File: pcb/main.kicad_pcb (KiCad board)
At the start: 2 copper layers, 257 x 76.2 mm, 110 parts, among them J1 Barrel_Jack, J2 NXC digit iface, J3 NXC num iface, J4 Conn_01x03, J5 ICSP, J6 Conn_02x06_Counter_Clockwise, J7 Conn_02x12_Counter_Clockwise, Q1 IRF740, Q10 ZVP1320F, Q11 BSS127S, Q12 ZVN3320F, Q13 BSS127S, Q14 BSS127S, Q15 ZVP1320F, Q16 BSS127S, Q17 BSS127S, Q18 ZVN3320F, Q19 BSS127S, Q2 ZVN3320F, Q20 ZVP1320F, Q3 BSS127S, Q4 ZVP1320F, Q5 BSS127S, Q6 BSS127S, Q7 ZVN3320F, Q8 BSS127S, Q9 BSS127S, SW1 Tactile SPST, SW2 Tactile SPST, SW3 Tactile SPST, U1 4028, U2 NCP1117-5.0_SOT223, U3 PIC24FV32KA302-I_SO, U4 DS1307Z+, U5 MAX1771, Y1 8 MHz, Y2 32.768 kHz

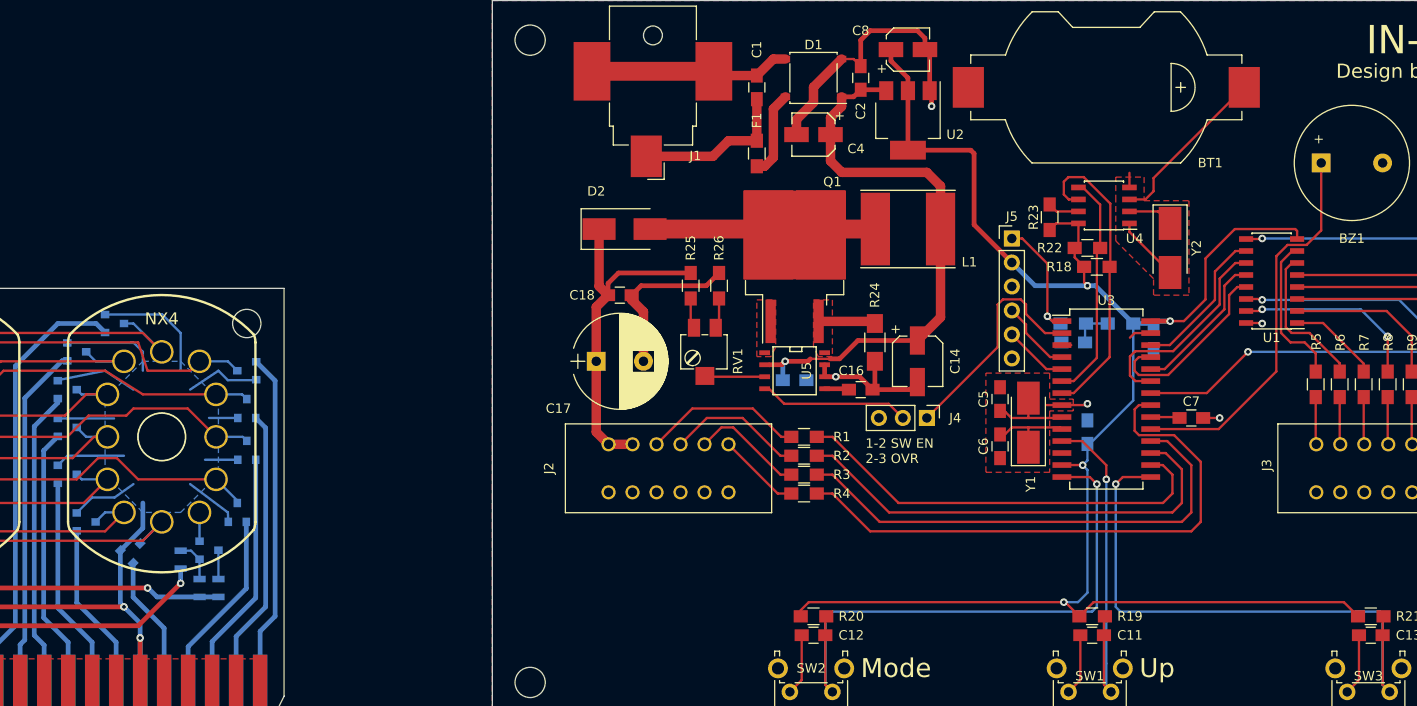
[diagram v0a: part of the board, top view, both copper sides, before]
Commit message: Update PCB and schematic files with mostly small tweaks. Added DRC rules added to .pro, and changes on layout and footprints to reflect that.
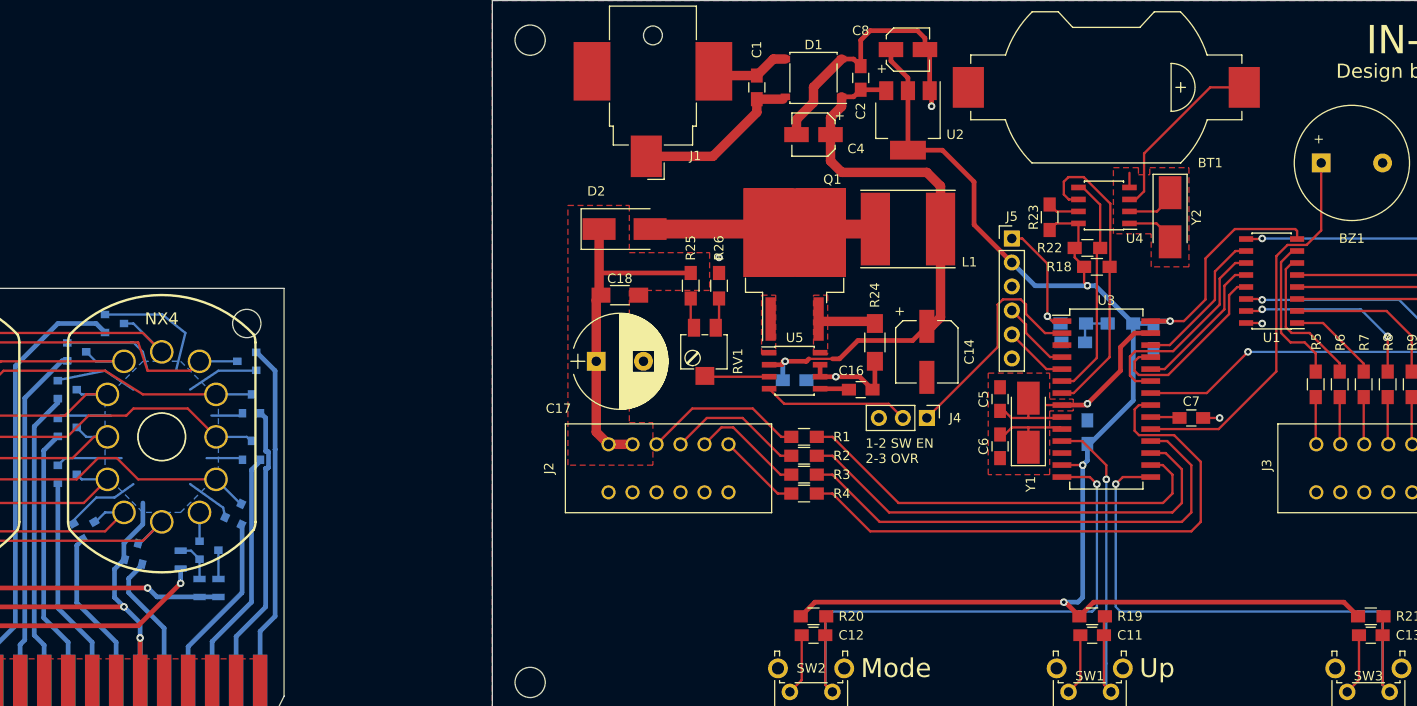
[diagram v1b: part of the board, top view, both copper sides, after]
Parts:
- removed F1: 1.5A, Resistors_SMD:R_0805_HandSoldering
- C14: footprint Capacitors_SMD:CP_Elec_5x5.3 -> Capacitors_SMD:CP_Elec_6.3x7.7
- C18: footprint Capacitors_SMD:C_0805_HandSoldering -> Capacitors_SMD:C_1206_HandSoldering
- R18, R22: value 33k -> 4.7k
- U1: value 4028 -> CD4028
- U2: value NCP1117-5.0_SOT223 -> NCP1117
- U5: footprint SMD_Packages:SOIC-8-N -> Housings_SOIC:SOIC-8_3.9x4.9mm_Pitch1.27mm
- moved Y2 3.25 mm to (221.8, 76.8)
- moved C14 1.41 mm to (196.0, 91.0)
- moved Q13 1.00 mm to (124.0, 92.0)
- moved Q14 0.71 mm to (124.5, 96.5)
- moved Q16 0.50 mm to (124.5, 101.4)
- moved Q3 0.50 mm to (107.0, 109.5), turned to 30 degrees
- moved Q19 0.35 mm to (112.2, 112.2), turned to 75 degrees
- moved Q1 0.25 mm to (182.0, 81.8)
- turned Q17 to 65 degrees
- turned U5 to 0 degrees
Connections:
- D1 pad 4: Net-(D1-Pad4) -> Net-(C1-Pad1)
- J1 pad 3: Net-(C1-Pad2) -> Net-(J1-Pad3)
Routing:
- net /GND: track 94.3 -> 80.8 mm, vias 5 -> 6
- net Net-(C1-Pad2): track 21.4 -> 8.49 mm
- net Net-(D1-Pad4): track 9.09 -> 0.00 mm
- net /+5V: track 183.6 -> 181.1 mm
- net Net-(U4-Pad1): track 6.98 -> 5.41 mm
- net Net-(BT1-Pad1): track 17.9 -> 19.4 mm
- net Net-(C1-Pad1): track 16.8 -> 18.2 mm
- net /+170V: track 37.2 -> 35.9 mm
- net /Tube Board/K7: track 35.4 -> 36.5 mm
- net /Tube Board/GND: track 206.8 -> 207.9 mm
- net Net-(U3-Pad3): track 0.98 -> 0.00 mm
- net /Tube Board/K1: track 17.8 -> 16.9 mm
- net /Tube Board/K8: track 29.7 -> 30.5 mm
- net /+RAW: track 61.3 -> 62.1 mm
- net /Tube Board/K_DP: track 14.0 -> 14.7 mm
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
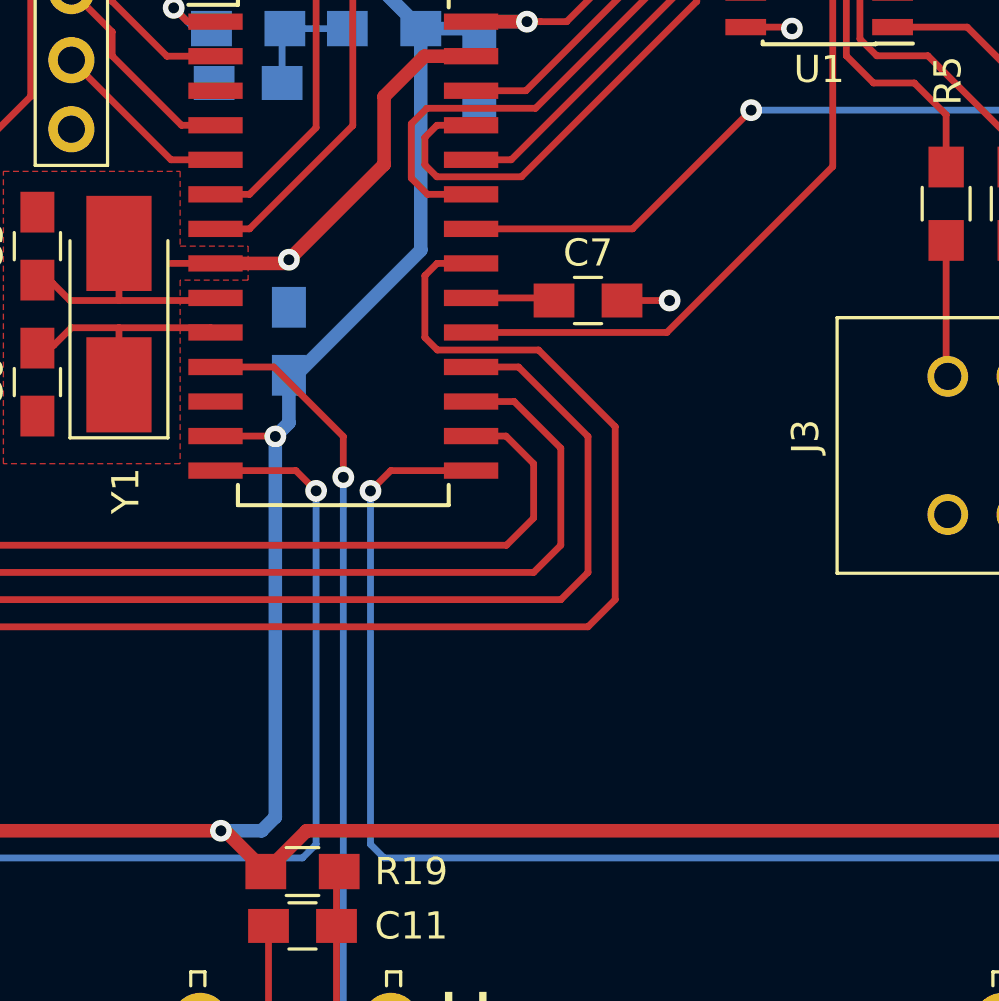
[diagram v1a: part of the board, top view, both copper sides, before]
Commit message: Add alternate parts for BOM, adjust micro to be more compatible with new PIC24FJ series parts.
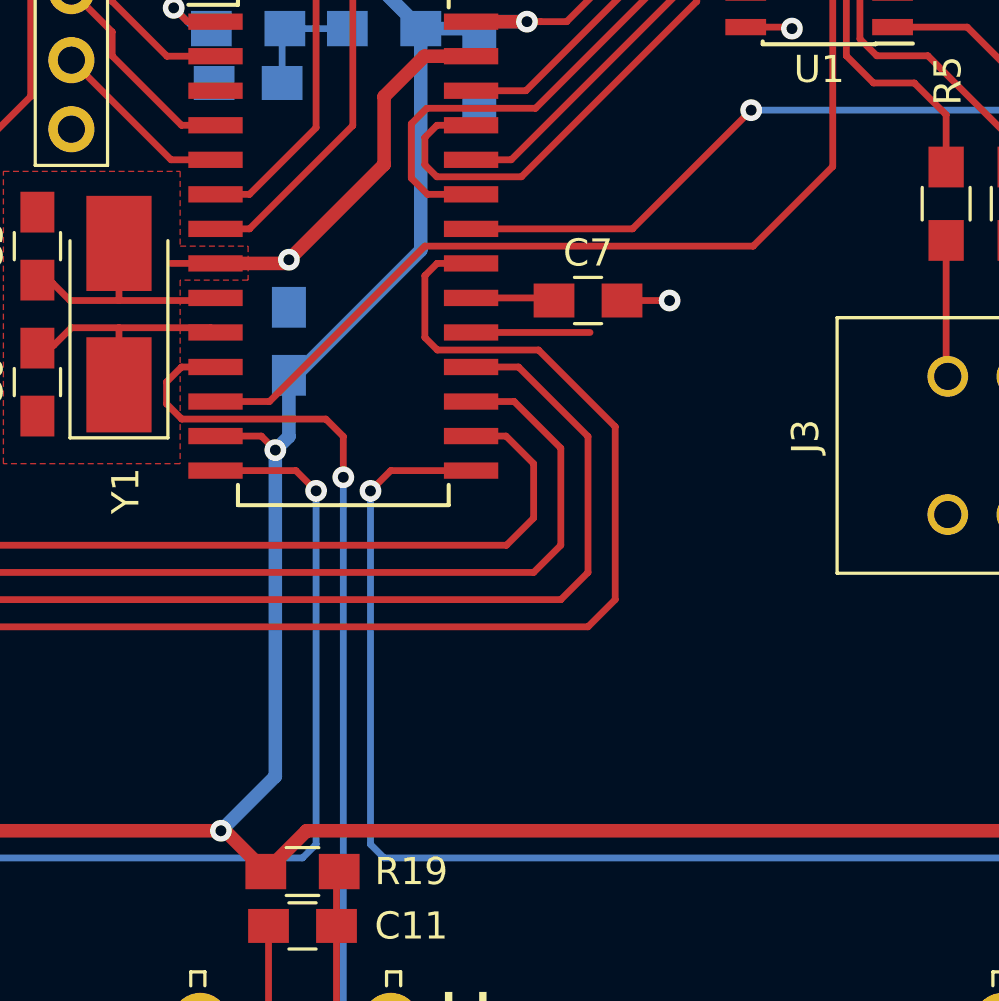
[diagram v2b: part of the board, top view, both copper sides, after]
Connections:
- U3 pad 12: Net-(U3-Pad12) -> /BUZZ
- U3 pad 19: /BUZZ -> /GND
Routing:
- net /BUZZ: track 40.8 -> 51.3 mm
- net /GND: track 80.8 -> 85.2 mm
- net /UP_SW: track 38.3 -> 42.4 mm
- net /+5V: track 181.1 -> 180.4 mm

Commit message: Update schematic with some better part selection, reducing BOM. Update PCB for panelized fabrication.
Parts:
- C1: value 0.01u -> 0.1u
- C14: footprint Capacitors_SMD:CP_Elec_6.3x7.7 -> Capacitors_SMD:CP_Elec_6.3x5.8
- R18, R22: value 4.7k -> 2.2k
- R25: value 1.5M -> 1M
- R26: value 13.3k -> 2.2k
- moved H5 82.5 mm to (104.0, 108.0)
- moved H6 82.5 mm to (204.0, 108.0)
- moved J6 82.5 mm to (108.9, 142.4)
- moved J7 82.5 mm to (191.4, 142.4)
- moved NX1 82.5 mm to (112.7, 120.0)
- moved NX2 82.5 mm to (138.0, 120.0)
- moved NX3 82.5 mm to (170.0, 120.0)
- moved NX4 82.5 mm to (195.0, 120.0)
- moved Q10 82.5 mm to (142.0, 133.0)
- moved Q11 82.5 mm to (190.0, 108.0)
- moved Q12 82.5 mm to (166.0, 134.0)
- moved Q13 82.5 mm to (204.0, 112.0)
- moved Q14 82.5 mm to (204.5, 116.5)
- moved Q15 82.5 mm to (174.0, 133.0)
- moved Q16 82.5 mm to (204.5, 121.4)
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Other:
- board size 257 x 76.2 mm -> 127 x 122.2 mm

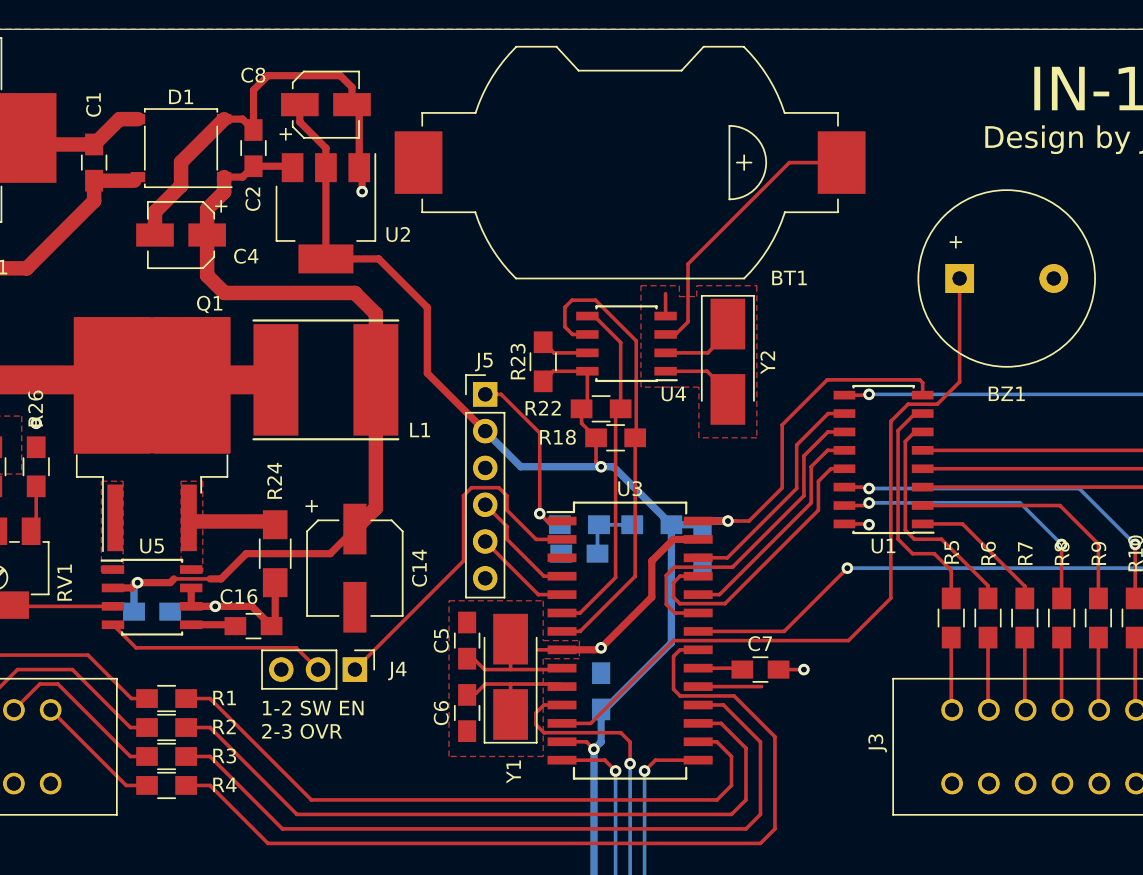
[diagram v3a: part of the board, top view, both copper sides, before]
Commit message: Fix some problems with pcb, crystals and rectifier using wrong footprints. Octal decoder had Vss and Vdd swapped.
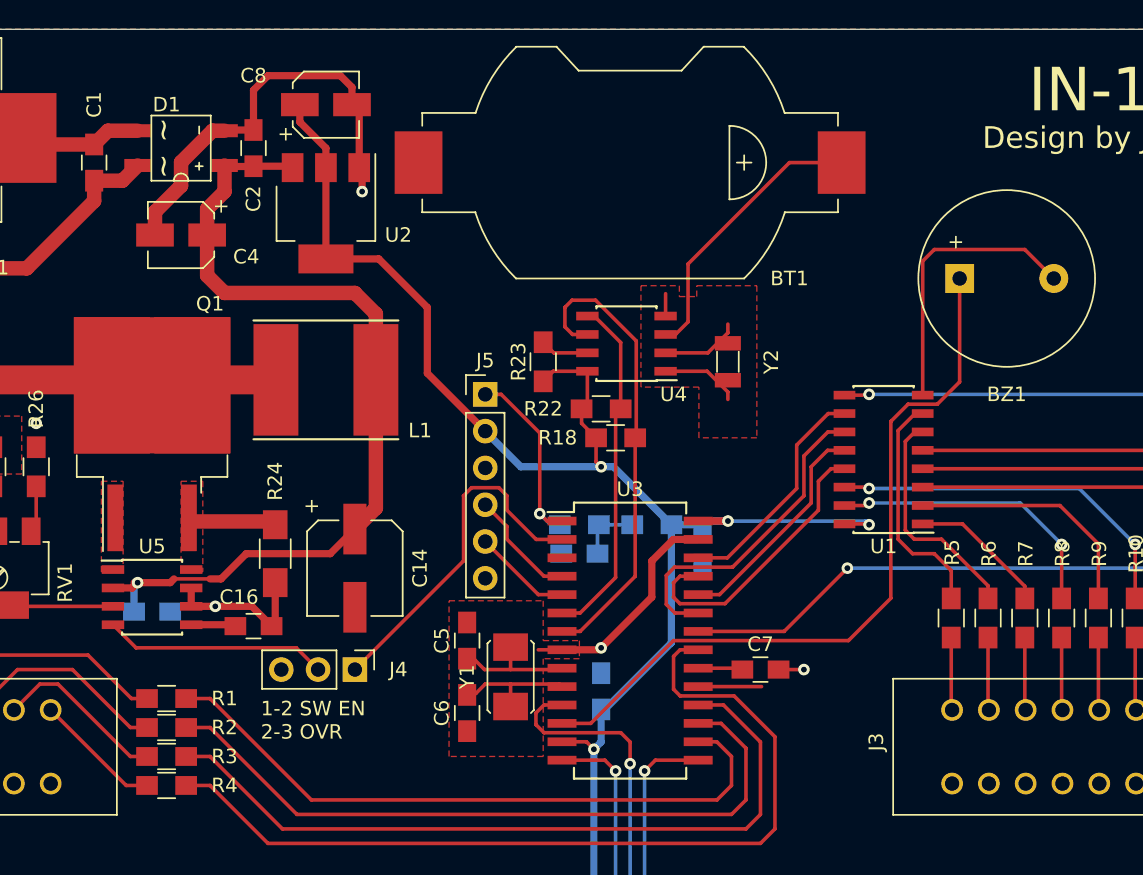
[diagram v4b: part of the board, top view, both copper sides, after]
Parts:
- D1: footprint Diodes_SMD:Diode_Bridge_MBLS -> nixie-clock:Diode-SMC_KMB22S-MBS
- Y1: footprint Crystals:Crystal_SMD_5032-2pin_5.0x3.2mm_HandSoldering -> nixie-clock:Crystal-Abracom_ABM3-5.0x3.2
- Y2: footprint Crystals:Crystal_SMD_5032-2pin_5.0x3.2mm_HandSoldering -> nixie-clock:Crystal-Vectron_VMK3-3.2x1.5
- turned D1 to 270 degrees
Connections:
- U1 pad 16: /GND -> /+5V
- U1 pad 8: /+5V -> /GND
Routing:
- net /GND: track 85.2 -> 102.3 mm, vias 6 -> 5
- net /+5V: track 180.4 -> 171.0 mm, vias 4 -> 5
